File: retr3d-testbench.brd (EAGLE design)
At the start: 101.9 x 53.3 mm, 72 parts, among them U1 ARDUINO-MEGAFULL

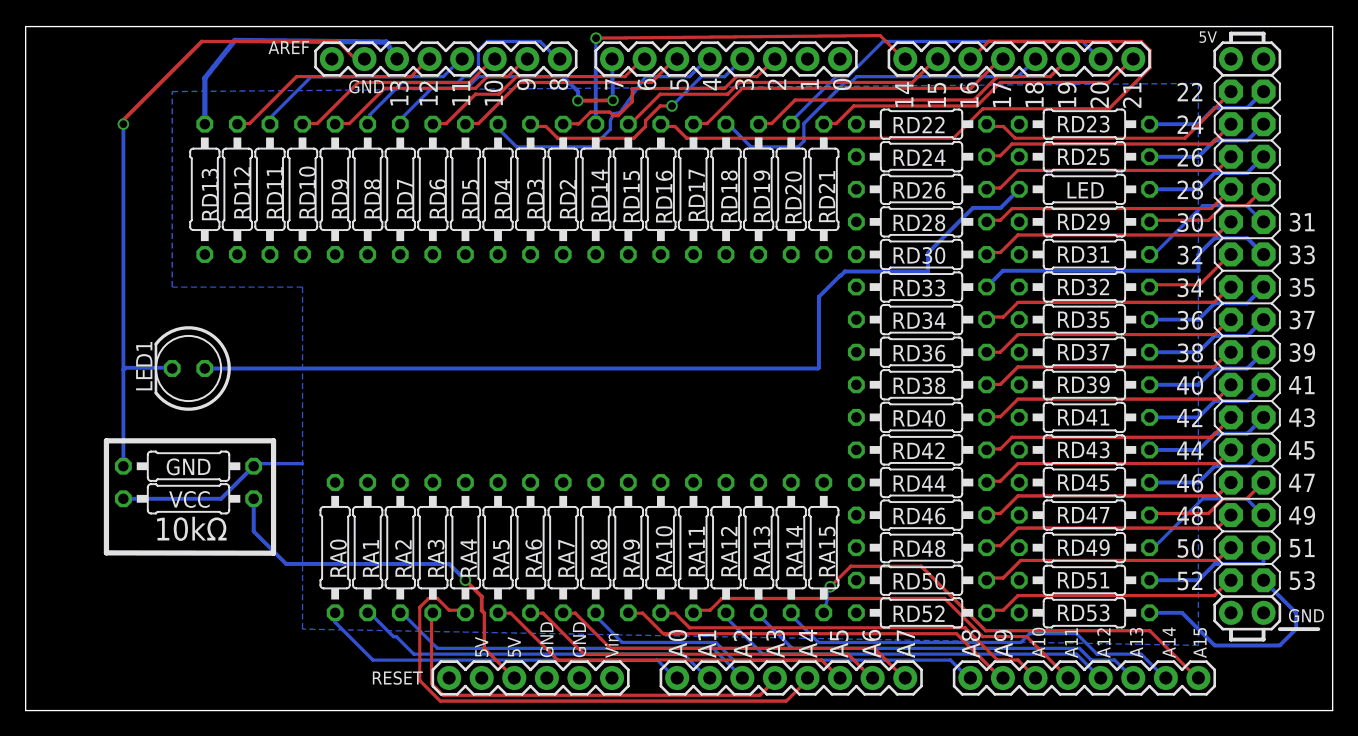
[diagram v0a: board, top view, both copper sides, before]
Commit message: Added SMD one sided version
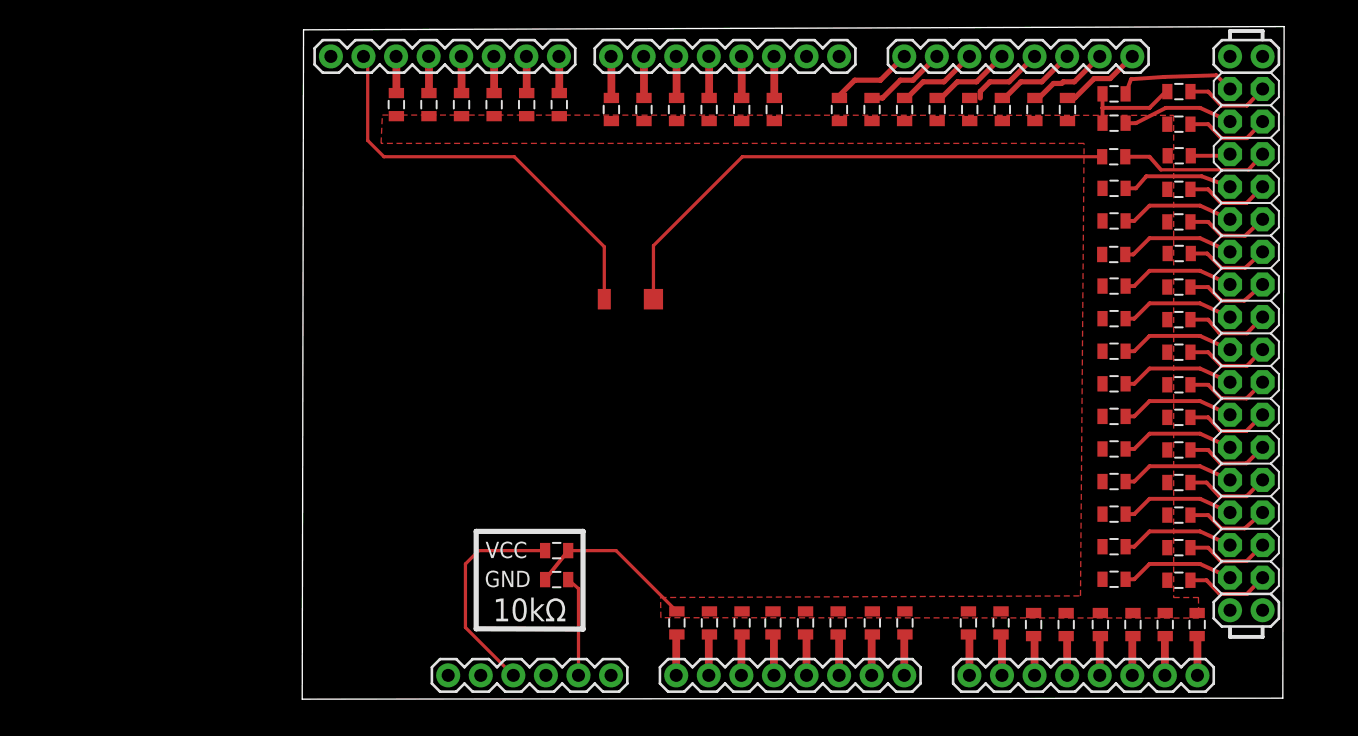
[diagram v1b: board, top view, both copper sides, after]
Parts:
- GND, LED, RA0, RA1, RA10, RA11, RA12, RA13, RA14, RA15, RA2, RA3, RA4, RA5, RA6, RA7, RA8, RA9, RD10, RD11, RD12, RD13, RD14, RD15, RD16, RD17, RD18, RD19, RD2, RD20, RD21, RD22, RD23, RD24, RD25, RD26, RD28, RD29, RD3, RD30, RD31, RD32, RD33, RD34, RD35, RD36, RD37, RD38, RD39, RD4, RD40, RD41, RD42, RD43, RD44, RD45, RD46, RD47, RD48, RD49, RD5, RD50, RD51, RD52, RD53, RD6, RD7, RD8, RD9, VCC: device eagle-ltspice:0207/10 -> SparkFun-Resistors:0805
- LED1: device led:LED5MM -> masterperson40:LED-1206-BOTTOM
- U1: value ARDUINO-MEGAFULL -> ARDUINO-MEGAARDUINO_MEGA_MINIMAL; device SparkFun-Boards:ARDUINO_MEGA -> masterperson40:ARDUINO_MEGA
- moved U1 116.0 mm to (102.8, 73.9)
- moved GND 30.0 mm to (42.7, 28.0), turned to 0 degrees
- moved RA12 29.8 mm to (85.1, 24.5)
- moved RA13 29.8 mm to (87.6, 24.5)
- moved RA14 29.8 mm to (90.1, 24.5)
- moved RA15 29.7 mm to (92.6, 24.5)
- moved RA10 29.7 mm to (79.9, 24.5)
- moved RA11 29.7 mm to (82.4, 24.5)
- moved RA8 29.6 mm to (74.8, 24.6)
- moved RA9 29.6 mm to (77.3, 24.6)
- moved VCC 29.0 mm to (42.7, 30.3), turned to 180 degrees
- moved RA0 27.3 mm to (52.0, 24.6)
- moved RA7 27.3 mm to (69.8, 24.6)
- moved RA1 27.3 mm to (54.6, 24.6)
- moved RA2 27.3 mm to (57.1, 24.6)
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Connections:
- new net N$6: LED1.C, U1.GND@4
- net GND: now also U1.GND@1; no longer LED1.K, U1.GND@4
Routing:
- net N$50: track 57.1 -> 6.40 mm
- net GND: track 52.9 -> 7.83 mm, vias 1 -> 0
- net N$11: track 41.8 -> 3.27 mm
- net N$6: track 0.00 -> 32.7 mm
- net N$27: track 35.1 -> 3.09 mm, vias 1 -> 0
- net N$5: track 73.4 -> 42.0 mm
- net N$174: track 33.4 -> 3.27 mm
- net N$21: track 32.3 -> 3.14 mm
- net N$26: track 32.0 -> 3.09 mm
- net N$23: track 31.6 -> 3.11 mm
- net N$24: track 31.4 -> 3.11 mm
- net N$17: track 31.5 -> 3.27 mm
- net N$20: track 31.3 -> 3.14 mm
- net N$192: track 31.3 -> 3.27 mm
- net N$4: track 29.2 -> 3.24 mm
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- added copper zone on layer 1, net N$TEST
- removed copper zone on layer 16, net N$TEST
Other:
- board size 101.9 x 53.3 mm -> 76.6 x 52.4 mm
- board text removed: "C:/Users/Master/Git/retr3d/docs/retr3dSilkscreen-testbench.bmp"
- board text removed: "C:/Users/Master/Git/retr3d/docs/retr3dSilkscreen.bmp"
- board text removed: "For assembly and usage goto"
